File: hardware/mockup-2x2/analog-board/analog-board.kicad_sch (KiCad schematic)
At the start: 135 parts, among them J1 12V, J2 COIL JOINT, J4 MCU, J5 PI ZERO, Q1 AO3401A, Q11 AO3400A, Q12 AO3400A, Q13 AO3400A, Q14 AO3400A, Q2 AO3400A, Q21 AO3401A, Q22 AO3401A, Q23 AO3401A, Q24 AO3401A, U1 TPS62150, U2 LP2985-5.0, U3 74HC4052, U4 AD8421, U5 OPA2810, U6 OPA2810, U7 ADuM1201

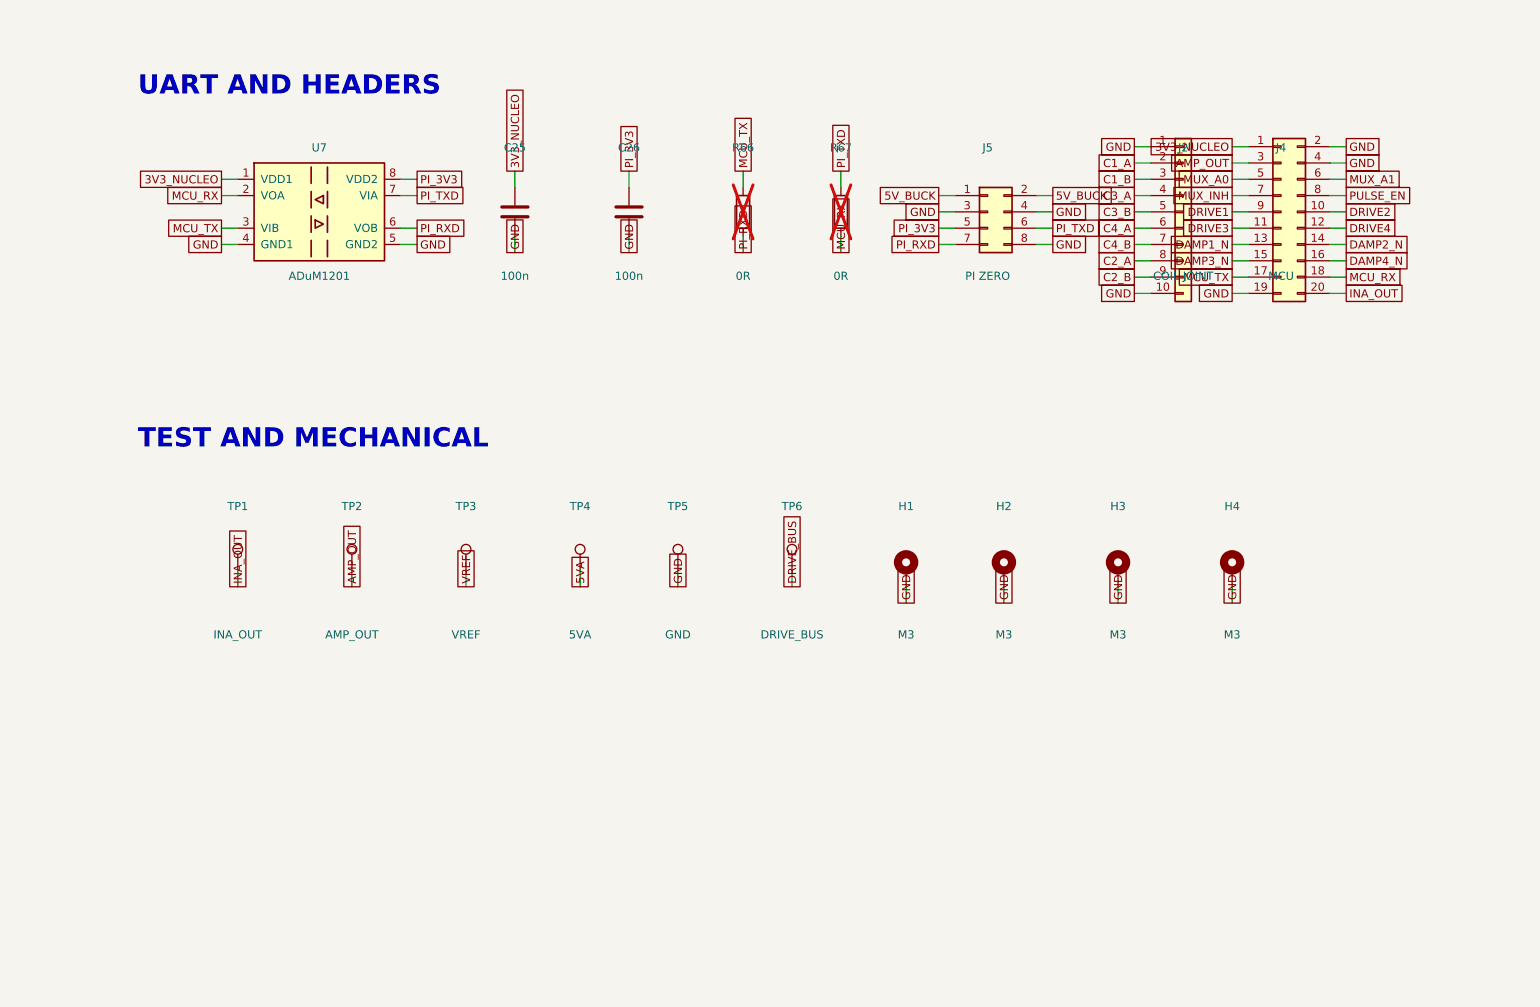
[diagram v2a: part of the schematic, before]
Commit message: Reference LED complete : cartes, gabarit bois, protocole, docs
Carte analogique regeneree avec le tampon deplace pres du connecteur
MCU : les nets LED (donnees, tampon, 5V vers le joint 12 broches)
sont entierement routes, 499 pistes, 259 vias, DRC zero, 12 jonctions
de finition posees ; restent les sept couloirs satures connus de la
bande des cellules et du coin buck, listes dans le README de la
carte. Gabarit de percage surface-template (contour carte, visserie,
deux points lumineux par case) genere par la mecanique et exporte.
Protocole : M10 bois contre acrylique, M11 bruit des LED. ADR 0009
(LED de camp et surface bois) indexe, READMEs et fiche
d'approvisionnement mis a jour (lignes WS2812B et tampon, assemblage
des deux cartes, totaux revises, contreplaque au lieu d'acrylique).
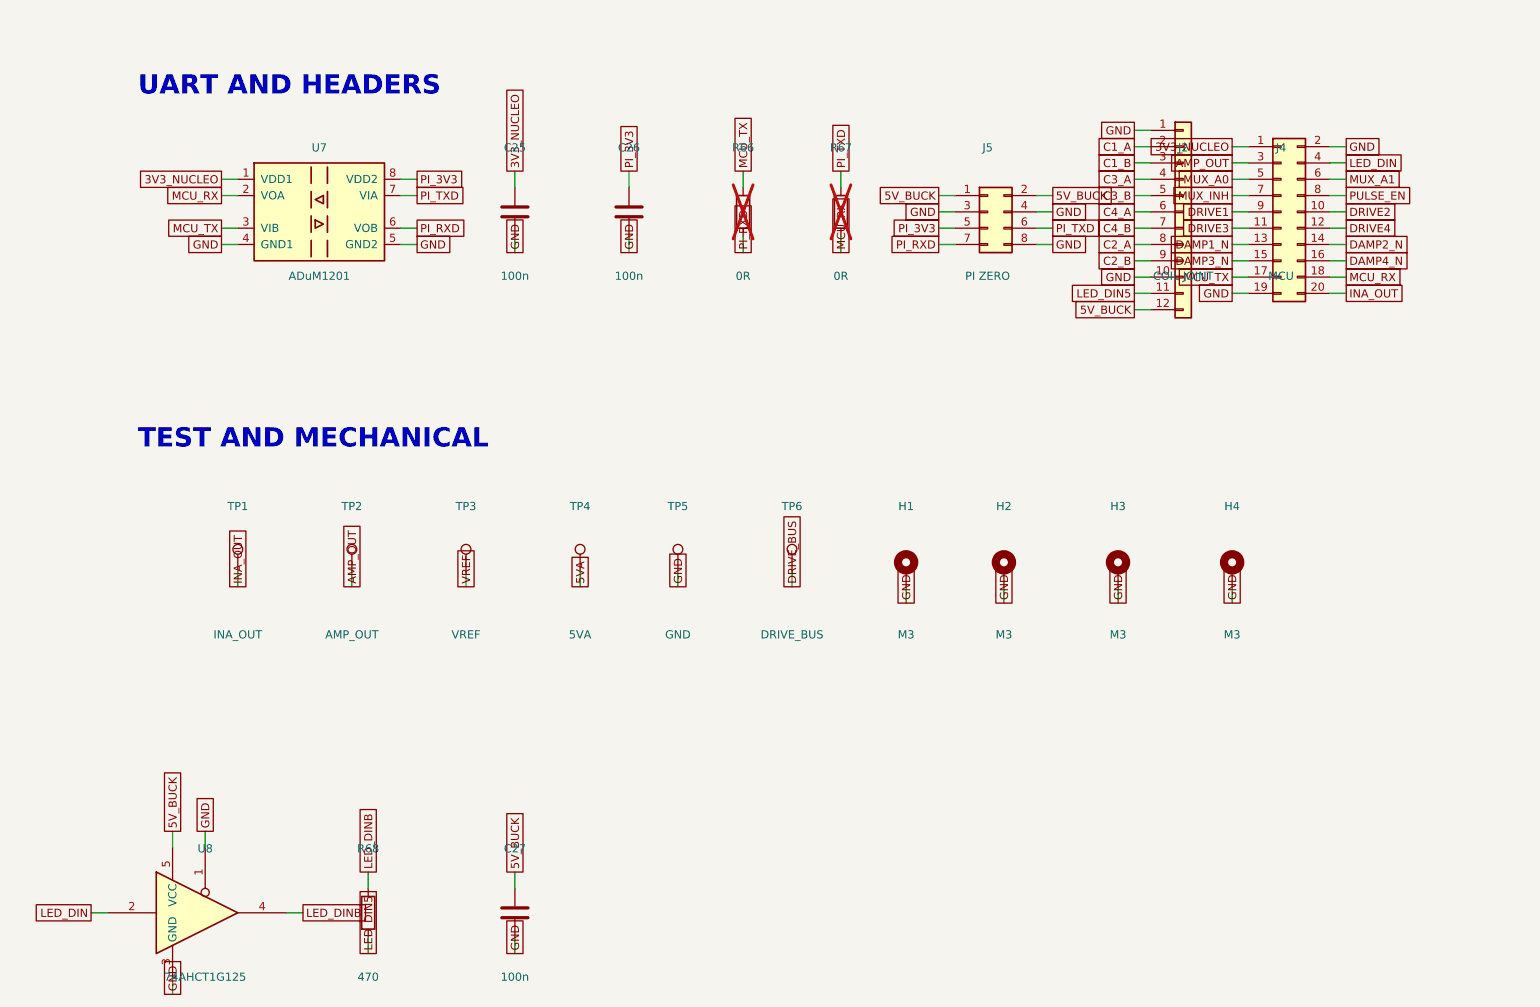
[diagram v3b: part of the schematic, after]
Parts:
- removed J2: COIL JOINT, Connector_PinHeader_2.54mm:PinHeader_1x10_P2.54mm_Vertical, symbol Connector_Generic:Conn_01x10
- added C27: 100n, Capacitor_SMD:C_0603_1608Metric, symbol Device:C
- added J2: COIL JOINT, Connector_PinHeader_2.54mm:PinHeader_1x12_P2.54mm_Vertical, symbol Connector_Generic:Conn_01x12
- added R68: 470, Resistor_SMD:R_0603_1608Metric, symbol Device:R
- added U8: 74AHCT1G125, Package_TO_SOT_SMD:SOT-23-5, symbol 74xGxx:74LVC1G125
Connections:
- net 5V_BUCK: now also C27.1, J2.12 (Pin_12), U8.5 (VCC)
- net C1_A: now also J2.2 (Pin_2)
- net C1_B: now also J2.3 (Pin_3)
- net C2_A: now also J2.8 (Pin_8)
- net C2_B: now also J2.9 (Pin_9)
- net C3_A: now also J2.4 (Pin_4)
- net C3_B: now also J2.5 (Pin_5)
- net C4_A: now also J2.6 (Pin_6)
- net C4_B: now also J2.7 (Pin_7)
- net GND: now also C27.2, J2.1 (Pin_1), J2.10 (Pin_10), U8.1, U8.3 (GND); no longer J4.4 (Pin_4)
- new net LED_DIN: J4.4 (Pin_4), U8.2
- new net LED_DIN5: J2.11 (Pin_11), R68.2
- new net LED_DINB: R68.1, U8.4

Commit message: Carte analogique de maquette : les vingt-huit liaisons fermées
Le compte du build disait sept liaisons ouvertes, KiCad en comptait
vingt-huit. L'arbitre était faux : le modèle de connexité ignorait la
masse, fusionnait les deux couches sans exiger de via et prenait la
boîte d'une pastille pour son cuivre. Il est remplacé par le modèle
exact du quadrant, forme vraie des pastilles comprise, avec le plan de
masse calculé comme le calcule le remplisseur de KiCad, îlot par îlot.
Le compte du build est désormais celui de KiCad, vérifié sur l'ancien
fichier comme sur le nouveau.

Dix-neuf des vingt-huit manquants étaient des masses : des groupes de
pastilles reliés en face avant mais jamais descendus vers un îlot que
le plan garde entier. Une passe de finition de la masse, jouée contre
les îlots réels, les ferme ; elle ne déplace pas le plan, puisque le
cuivre de masse n'est pas étranger au sien.

Pour le reste, deux outils. Un labyrinthe à géométrie exacte, trame de
0,05 mm sur les deux couches, via et coude payants, qui ferme ce
qu'aucun raccord droit ne ferme, dont une nappe de 25 mm. Et treize
routes structurelles tracées avant le routage dans des canaux mesurés
libres de pastilles, chacune revérifiée au build : les deux lignes de
cellule, la prise A de la cellule 2, deux broches du multiplexeur, la
résistance de fuite de la cellule 1, les deux sorties du régulateur, et
quatre masses que le plan n'atteint pas, dont un bus le long du bord
sud pour le connecteur de bobines.

La garde des raccords passe de 0,132 à 0,15 mm, la valeur de la classe
de nets : le DRC de KiCad comptait les 0,138 comme des erreurs.

Résultat mesuré : 557 pistes, 296 vias, zéro élément non connecté au
DRC de KiCad comme au compte du build. Restent deux défauts de
placement, hérités et documentés : 49 chevauchements de courtyard et
la broche 2 du jack J1, 1 mm hors du contour.
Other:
- note added: "OTHER"
